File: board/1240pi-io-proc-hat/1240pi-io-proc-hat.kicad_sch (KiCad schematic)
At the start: 6 parts

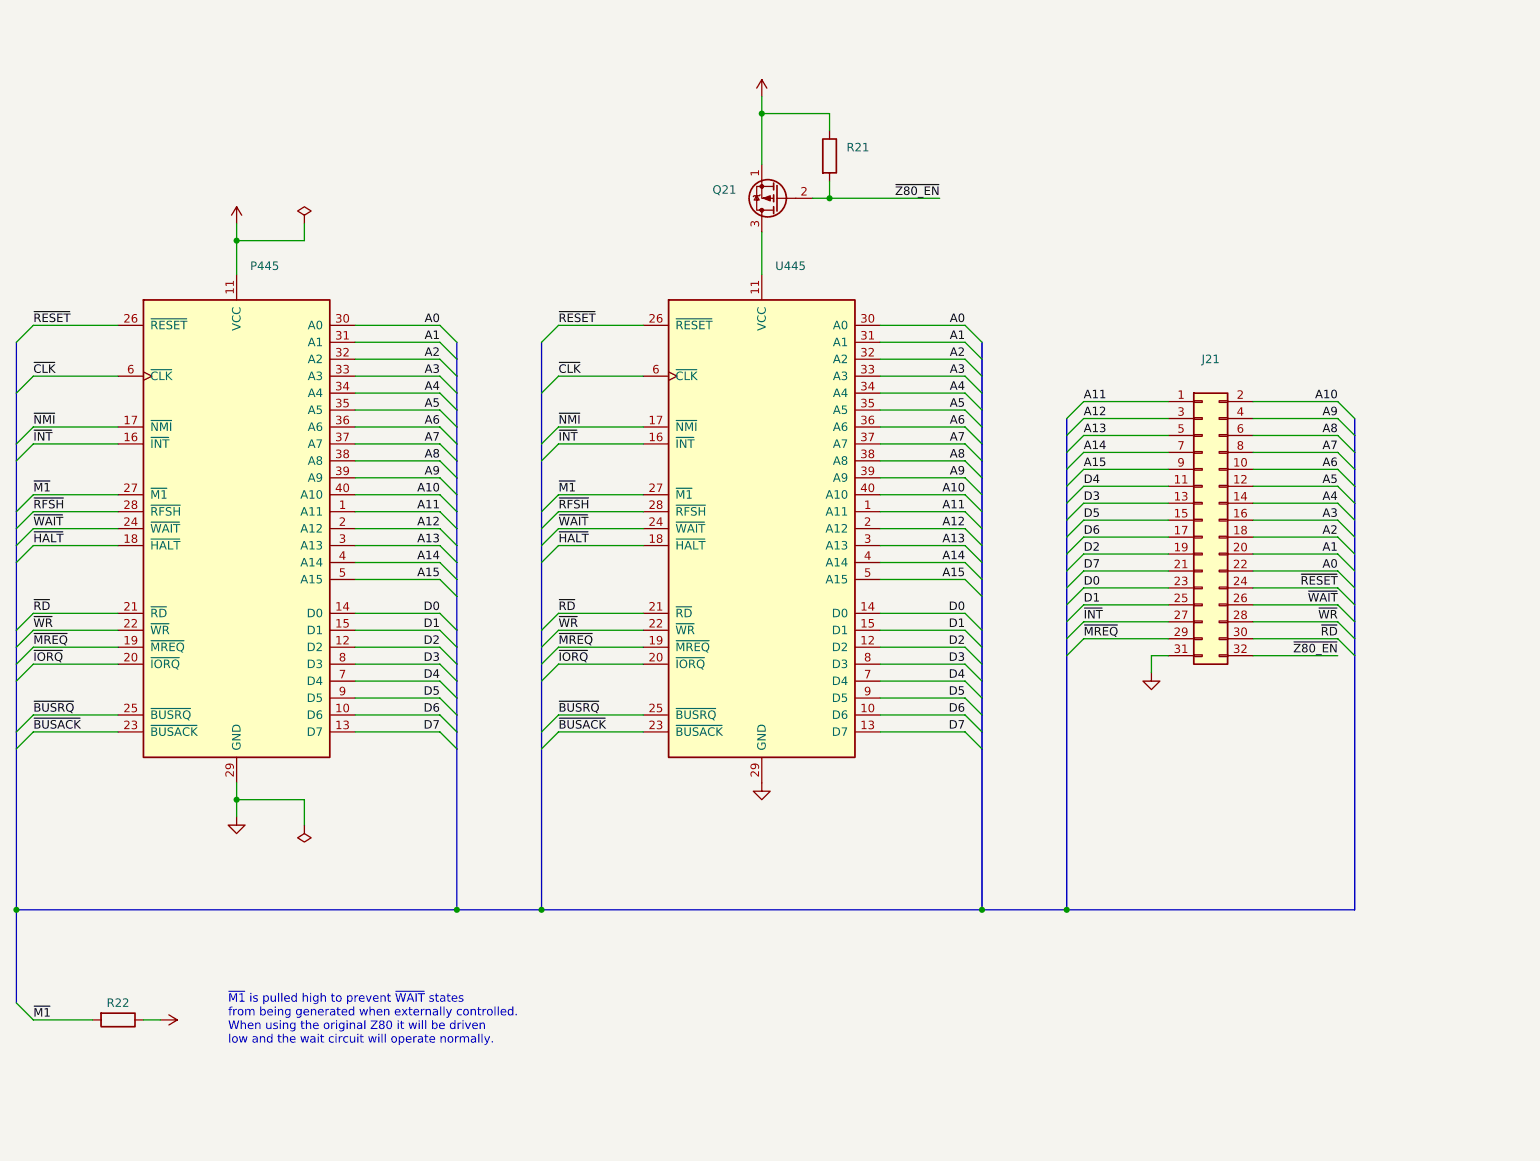
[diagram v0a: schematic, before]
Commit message: Split hats into separate projects / boards.
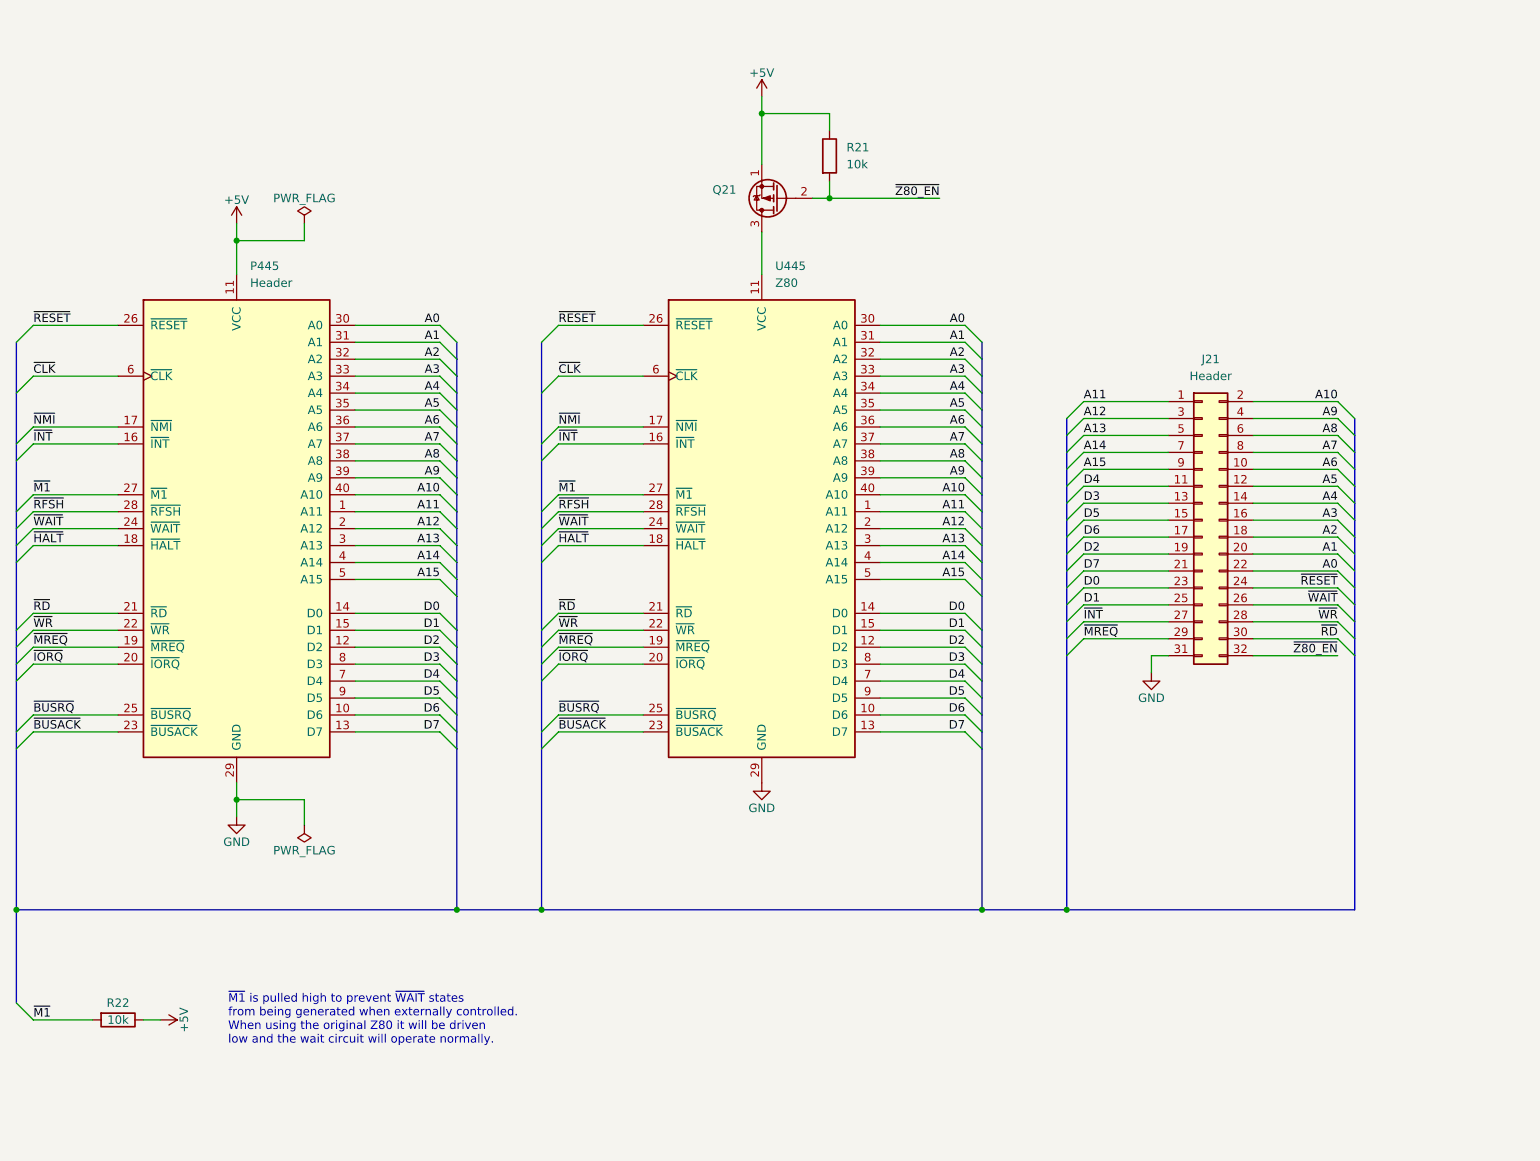
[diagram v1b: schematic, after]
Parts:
- J21: value (none) -> Header; footprint (none) -> Connector_PinHeader_2.54mm:PinHeader_2x16_P2.54mm_Vertical
- P445: value (none) -> Header; footprint (none) -> Package_DIP:DIP-40_W15.24mm
- Q21: value (none) -> ~; footprint (none) -> Package_TO_SOT_THT:TO-92_Wide
- R21, R22: value (none) -> 10k; footprint (none) -> Resistor_THT:R_Axial_DIN0207_L6.3mm_D2.5mm_P10.16mm_Horizontal
- U445: value (none) -> Z80; footprint (none) -> Package_DIP:DIP-40_W15.24mm_Socket
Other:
- title: 1240-Pi Modification Boards -> 1240-Pi I/O Processor Mod
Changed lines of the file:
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@@
   (paper "USLetter")
   (title_block
-    (title "1240-Pi Modification Boards")
+    (title "1240-Pi I/O Processor Mod")
     (date "2022-04-21")
     (rev "1.0")
@@
   (symbol (lib_id "power:GND") (at 195.58 129.54 0) (unit 1)
     (in_bom yes) (on_board yes) (fields_autoplaced)
-    (property "Reference" "#PWR0111" (id 0) (at 195.58 135.89 0)
-      (effects (font (size 1.27 1.27)) hide)
-    )
-    (property "Value" "" (id 1) (at 195.58 134.62 0))
+    (property "Reference" "#PWR?" (id 0) (at 195.58 135.89 0)
+      (effects (font (size 1.27 1.27)) hide)
+    )
+    (property "Value" "GND" (id 1) (at 195.58 133.35 0))
     (property "Footprint" "" (id 2) (at 195.58 129.54 0)
       (effects (font (size 1.27 1.27)) hide)
@@
   (symbol (lib_id "power:GND") (at 137.16 146.05 0) (unit 1)
     (in_bom yes) (on_board yes) (fields_autoplaced)
-    (property "Reference" "#PWR0106" (id 0) (at 137.16 152.4 0)
-      (effects (font (size 1.27 1.27)) hide)
-    )
-    (property "Value" "~" (id 1) (at 137.16 151.13 0))
+    (property "Reference" "#PWR?" (id 0) (at 137.16 152.4 0)
+      (effects (font (size 1.27 1.27)) hide)
+    )
+    (property "Value" "GND" (id 1) (at 137.16 149.86 0))
     (property "Footprint" "" (id 2) (at 137.16 146.05 0)
       (effects (font (size 1.27 1.27)) hide)
@@
       (effects (font (size 1.27 1.27)) (justify left))
     )
-    (property "Value" "" (id 1) (at 149.86 53.3399 0)
+    (property "Value" "10k" (id 1) (at 149.86 53.3399 0)
       (effects (font (size 1.27 1.27)) (justify left))
     )
-    (property "Footprint" "" (id 2) (at 145.542 52.07 90)
+    (property "Footprint" "Resistor_THT:R_Axial_DIN0207_L6.3mm_D2.5mm_P10.16mm_Horizontal" (id 2) (at 145.542 52.07 90)
       (effects (font (size 1.27 1.27)) hide)
     )
@@
       (effects (font (size 1.27 1.27)) (justify left))
     )
-    (property "Value" "" (id 1) (at 139.1794 71.12 0)
+    (property "Value" "Z80" (id 1) (at 139.1794 71.12 0)
       (effects (font (size 1.27 1.27)) (justify left))
     )
-    (property "Footprint" "" (id 2) (at 137.16 97.79 0)
+    (property "Footprint" "Package_DIP:DIP-40_W15.24mm_Socket" (id 2) (at 137.16 97.79 0)
       (effects (font (size 1.27 1.27)) hide)
     )
@@
   (symbol (lib_id "power:+5V") (at 46.99 181.61 270) (unit 1)
     (in_bom yes) (on_board yes) (fields_autoplaced)
-    (property "Reference" "#PWR0110" (id 0) (at 43.18 181.61 0)
-      (effects (font (size 1.27 1.27)) hide)
-    )
-    (property "Value" "" (id 1) (at 52.07 181.61 0))
+    (property "Reference" "#PWR?" (id 0) (at 43.18 181.61 0)
+      (effects (font (size 1.27 1.27)) hide)
+    )
+    (property "Value" "+5V" (id 1) (at 50.546 181.61 0))
     (property "Footprint" "" (id 2) (at 46.99 181.61 0)
       (effects (font (size 1.27 1.27)) hide)
@@
   (symbol (lib_id "power:+5V") (at 137.16 43.18 0) (unit 1)
     (in_bom yes) (on_board yes) (fields_autoplaced)
-    (property "Reference" "#PWR0107" (id 0) (at 137.16 46.99 0)
-      (effects (font (size 1.27 1.27)) hide)
-    )
-    (property "Value" "" (id 1) (at 137.16 38.1 0))
+    (property "Reference" "#PWR?" (id 0) (at 137.16 46.99 0)
+      (effects (font (size 1.27 1.27)) hide)
+    )
+    (property "Value" "+5V" (id 1) (at 137.16 39.624 0))
     (property "Footprint" "" (id 2) (at 137.16 43.18 0)
       (effects (font (size 1.27 1.27)) hide)
@@
   (symbol (lib_id "power:PWR_FLAG") (at 68.58 152.4 180) (unit 1)
     (in_bom yes) (on_board yes) (fields_autoplaced)
-    (property "Reference" "#FLG0103" (id 0) (at 68.58 154.305 0)
-      (effects (font (size 1.27 1.27)) hide)
-    )
-    (property "Value" "" (id 1) (at 68.58 157.48 0))
+    (property "Reference" "#FLG?" (id 0) (at 68.58 154.305 0)
+      (effects (font (size 1.27 1.27)) hide)
+    )
+    (property "Value" "PWR_FLAG" (id 1) (at 68.58 156.21 0))
     (property "Footprint" "" (id 2) (at 68.58 152.4 0)
       (effects (font (size 1.27 1.27)) hide)
@@
   (symbol (lib_id "power:GND") (at 58.42 151.13 0) (unit 1)
     (in_bom yes) (on_board yes) (fields_autoplaced)
-    (property "Reference" "#PWR0109" (id 0) (at 58.42 157.48 0)
-      (effects (font (size 1.27 1.27)) hide)
-    )
-    (property "Value" "" (id 1) (at 58.42 156.21 0))
+    (property "Reference" "#PWR?" (id 0) (at 58.42 157.48 0)
+      (effects (font (size 1.27 1.27)) hide)
+    )
+    (property "Value" "GND" (id 1) (at 58.42 154.94 0))
     (property "Footprint" "" (id 2) (at 58.42 151.13 0)
       (effects (font (size 1.27 1.27)) hide)
@@
       (effects (font (size 1.27 1.27)) (justify left))
     )
-    (property "Value" "" (id 1) (at 133.35 59.6899 0)
+    (property "Value" "~" (id 1) (at 133.35 59.6899 0)
       (effects (font (size 1.27 1.27)) (justify left))
     )
-    (property "Footprint" "" (id 2) (at 134.62 60.96 0)
+    (property "Footprint" "Package_TO_SOT_THT:TO-92_Wide" (id 2) (at 134.62 60.96 0)
       (effects (font (size 1.27 1.27)) hide)
     )
@@
   (symbol (lib_id "power:+5V") (at 58.42 62.23 0) (unit 1)
     (in_bom yes) (on_board yes) (fields_autoplaced)
-    (property "Reference" "#PWR0108" (id 0) (at 58.42 66.04 0)
-      (effects (font (size 1.27 1.27)) hide)
-    )
-    (property "Value" "" (id 1) (at 58.42 57.15 0))
+    (property "Reference" "#PWR?" (id 0) (at 58.42 66.04 0)
+      (effects (font (size 1.27 1.27)) hide)
+    )
+    (property "Value" "+5V" (id 1) (at 58.42 58.674 0))
     (property "Footprint" "" (id 2) (at 58.42 62.23 0)
       (effects (font (size 1.27 1.27)) hide)
@@
       (effects (font (size 1.27 1.27)) (justify left))
     )
-    (property "Value" "" (id 1) (at 60.4394 71.12 0)
+    (property "Value" "Header" (id 1) (at 60.4394 71.12 0)
       (effects (font (size 1.27 1.27)) (justify left))
     )
-    (property "Footprint" "" (id 2) (at 58.42 97.79 0)
+    (property "Footprint" "Package_DIP:DIP-40_W15.24mm" (id 2) (at 58.42 97.79 0)
       (effects (font (size 1.27 1.27)) hide)
     )
@@
   (symbol (lib_id "power:PWR_FLAG") (at 68.58 62.23 0) (unit 1)
     (in_bom yes) (on_board yes) (fields_autoplaced)
-    (property "Reference" "#FLG0104" (id 0) (at 68.58 60.325 0)
-      (effects (font (size 1.27 1.27)) hide)
-    )
-    (property "Value" "" (id 1) (at 68.58 57.15 0))
+    (property "Reference" "#FLG?" (id 0) (at 68.58 60.325 0)
+      (effects (font (size 1.27 1.27)) hide)
+    )
+    (property "Value" "PWR_FLAG" (id 1) (at 68.58 58.42 0))
     (property "Footprint" "" (id 2) (at 68.58 62.23 0)
       (effects (font (size 1.27 1.27)) hide)
@@
     (in_bom yes) (on_board yes)
     (property "Reference" "R22" (id 0) (at 40.64 179.07 90))
-    (property "Value" "" (id 1) (at 40.64 181.61 90))
-    (property "Footprint" "" (id 2) (at 40.64 179.832 90)
+    (property "Value" "10k" (id 1) (at 40.64 181.61 90))
+    (property "Footprint" "Resistor_THT:R_Axial_DIN0207_L6.3mm_D2.5mm_P10.16mm_Horizontal" (id 2) (at 40.64 179.832 90)
       (effects (font (size 1.27 1.27)) hide)
     )
@@
     (in_bom yes) (on_board yes) (fields_autoplaced)
     (property "Reference" "J21" (id 0) (at 204.47 82.55 0))
-    (property "Value" "" (id 1) (at 204.47 85.09 0))
-    (property "Footprint" "" (id 2) (at 203.2 106.68 0)
+    (property "Value" "Header" (id 1) (at 204.47 85.09 0))
+    (property "Footprint" "Connector_PinHeader_2.54mm:PinHeader_2x16_P2.54mm_Vertical" (id 2) (at 203.2 106.68 0)
       (effects (font (size 1.27 1.27)) hide)
     )
@@
     (pin "9")
   )
+  (sheet_instances
+    (path "/" (page "1"))
+  )
+  (symbol_instances
+    (path "/541631f1-5c6b-4984-b80b-da5d814ddc2a"
+      (reference "#FLG?") (unit 1) (value "PWR_FLAG") (footprint "")
+    )
+    (path "/b59ec72b-cbb3-4a84-b409-cb1a12e8909e"
+      (reference "#FLG?") (unit 1) (value "PWR_FLAG") (footprint "")
+    )
+    (path "/2aecf130-835d-43a0-a6c9-612e14e7a782"
+      (reference "#PWR?") (unit 1) (value "GND") (footprint "")
+    )
+    (path "/34c1fa01-b507-49e3-9b9f-c468b6e77596"
+      (reference "#PWR?") (unit 1) (value "GND") (footprint "")
+    )
+    (path "/53181a90-a010-4b72-99ae-37b5bd3dc882"
+      (reference "#PWR?") (unit 1) (value "+5V") (footprint "")
+    )
+    (path "/534827d0-458c-4104-bc6d-0255ad697b4c"
+      (reference "#PWR?") (unit 1) (value "+5V") (footprint "")
+    )
+    (path "/57c4d56d-de84-4172-ae0f-4c05a32da8d4"
+      (reference "#PWR?") (unit 1) (value "GND") (footprint "")
+    )
+    (path "/805d731d-4180-4b8e-bf12-b88ccec030b8"
+      (reference "#PWR?") (unit 1) (value "+5V") (footprint "")
+    )
+    (path "/f05fcee9-4158-40f8-b265-71b19b598390"
+      (reference "J21") (unit 1) (value "Header") (footprint "Connector_PinHeader_2.54mm:PinHeader_2x16_P2.54mm_Vertical")
+    )
+    (path "/8ad53c83-e421-4c0e-b4e0-361c324d4d58"
+      (reference "P445") (unit 1) (value "Header") (footprint "Package_DIP:DIP-40_W15.24mm")
+    )
+    (path "/6c1a4460-5fc9-4b10-afd6-ed10a018878d"
+      (reference "Q21") (unit 1) (value "~") (footprint "Package_TO_SOT_THT:TO-92_Wide")
+    )
+    (path "/39bc262a-7fca-4f46-a771-f7dcdf7ac0b0"
+      (reference "R21") (unit 1) (value "10k") (footprint "Resistor_THT:R_Axial_DIN0207_L6.3mm_D2.5mm_P10.16mm_Horizontal")
+    )
+    (path "/e1046c61-4f21-4849-8a9a-39f81b175891"
+      (reference "R22") (unit 1) (value "10k") (footprint "Resistor_THT:R_Axial_DIN0207_L6.3mm_D2.5mm_P10.16mm_Horizontal")
+    )
+    (path "/3a29e5d6-689f-46d7-a623-bc932a7056da"
+      (reference "U445") (unit 1) (value "Z80") (footprint "Package_DIP:DIP-40_W15.24mm_Socket")
+    )
+  )
 )

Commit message: Add hat boards to Aisler.
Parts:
- Q21: value ~ -> (none)
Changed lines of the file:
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@@
   (symbol (lib_id "power:GND") (at 195.58 129.54 0) (unit 1)
     (in_bom yes) (on_board yes) (fields_autoplaced)
-    (property "Reference" "#PWR?" (id 0) (at 195.58 135.89 0)
+    (property "Reference" "#PWR0104" (id 0) (at 195.58 135.89 0)
       (effects (font (size 1.27 1.27)) hide)
     )
@@
   (symbol (lib_id "power:GND") (at 137.16 146.05 0) (unit 1)
     (in_bom yes) (on_board yes) (fields_autoplaced)
-    (property "Reference" "#PWR?" (id 0) (at 137.16 152.4 0)
+    (property "Reference" "#PWR0106" (id 0) (at 137.16 152.4 0)
       (effects (font (size 1.27 1.27)) hide)
     )
@@
   (symbol (lib_id "power:+5V") (at 46.99 181.61 270) (unit 1)
     (in_bom yes) (on_board yes) (fields_autoplaced)
-    (property "Reference" "#PWR?" (id 0) (at 43.18 181.61 0)
+    (property "Reference" "#PWR0103" (id 0) (at 43.18 181.61 0)
       (effects (font (size 1.27 1.27)) hide)
     )
@@
   (symbol (lib_id "power:+5V") (at 137.16 43.18 0) (unit 1)
     (in_bom yes) (on_board yes) (fields_autoplaced)
-    (property "Reference" "#PWR?" (id 0) (at 137.16 46.99 0)
+    (property "Reference" "#PWR0105" (id 0) (at 137.16 46.99 0)
       (effects (font (size 1.27 1.27)) hide)
     )
@@
   (symbol (lib_id "power:PWR_FLAG") (at 68.58 152.4 180) (unit 1)
     (in_bom yes) (on_board yes) (fields_autoplaced)
-    (property "Reference" "#FLG?" (id 0) (at 68.58 154.305 0)
+    (property "Reference" "#FLG0102" (id 0) (at 68.58 154.305 0)
       (effects (font (size 1.27 1.27)) hide)
     )
@@
   (symbol (lib_id "power:GND") (at 58.42 151.13 0) (unit 1)
     (in_bom yes) (on_board yes) (fields_autoplaced)
-    (property "Reference" "#PWR?" (id 0) (at 58.42 157.48 0)
+    (property "Reference" "#PWR0102" (id 0) (at 58.42 157.48 0)
       (effects (font (size 1.27 1.27)) hide)
     )
@@
       (effects (font (size 1.27 1.27)) (justify left))
     )
-    (property "Value" "~" (id 1) (at 133.35 59.6899 0)
+    (property "Value" "" (id 1) (at 133.35 59.6899 0)
       (effects (font (size 1.27 1.27)) (justify left))
     )
@@
   (symbol (lib_id "power:+5V") (at 58.42 62.23 0) (unit 1)
     (in_bom yes) (on_board yes) (fields_autoplaced)
-    (property "Reference" "#PWR?" (id 0) (at 58.42 66.04 0)
+    (property "Reference" "#PWR0101" (id 0) (at 58.42 66.04 0)
       (effects (font (size 1.27 1.27)) hide)
     )
@@
   (symbol (lib_id "power:PWR_FLAG") (at 68.58 62.23 0) (unit 1)
     (in_bom yes) (on_board yes) (fields_autoplaced)
-    (property "Reference" "#FLG?" (id 0) (at 68.58 60.325 0)
+    (property "Reference" "#FLG0101" (id 0) (at 68.58 60.325 0)
       (effects (font (size 1.27 1.27)) hide)
     )
@@
   )
   (symbol_instances
+    (path "/b59ec72b-cbb3-4a84-b409-cb1a12e8909e"
+      (reference "#FLG0101") (unit 1) (value "PWR_FLAG") (footprint "")
+    )
     (path "/541631f1-5c6b-4984-b80b-da5d814ddc2a"
-      (reference "#FLG?") (unit 1) (value "PWR_FLAG") (footprint "")
-    )
-    (path "/b59ec72b-cbb3-4a84-b409-cb1a12e8909e"
-      (reference "#FLG?") (unit 1) (value "PWR_FLAG") (footprint "")
+      (reference "#FLG0102") (unit 1) (value "PWR_FLAG") (footprint "")
+    )
+    (path "/805d731d-4180-4b8e-bf12-b88ccec030b8"
+      (reference "#PWR0101") (unit 1) (value "+5V") (footprint "")
+    )
+    (path "/57c4d56d-de84-4172-ae0f-4c05a32da8d4"
+      (reference "#PWR0102") (unit 1) (value "GND") (footprint "")
+    )
+    (path "/53181a90-a010-4b72-99ae-37b5bd3dc882"
+      (reference "#PWR0103") (unit 1) (value "+5V") (footprint "")
     )
     (path "/2aecf130-835d-43a0-a6c9-612e14e7a782"
-      (reference "#PWR?") (unit 1) (value "GND") (footprint "")
+      (reference "#PWR0104") (unit 1) (value "GND") (footprint "")
+    )
+    (path "/534827d0-458c-4104-bc6d-0255ad697b4c"
+      (reference "#PWR0105") (unit 1) (value "+5V") (footprint "")
     )
     (path "/34c1fa01-b507-49e3-9b9f-c468b6e77596"
-      (reference "#PWR?") (unit 1) (value "GND") (footprint "")
-    )
-    (path "/53181a90-a010-4b72-99ae-37b5bd3dc882"
-      (reference "#PWR?") (unit 1) (value "+5V") (footprint "")
-    )
-    (path "/534827d0-458c-4104-bc6d-0255ad697b4c"
-      (reference "#PWR?") (unit 1) (value "+5V") (footprint "")
-    )
-    (path "/57c4d56d-de84-4172-ae0f-4c05a32da8d4"
-      (reference "#PWR?") (unit 1) (value "GND") (footprint "")
-    )
-    (path "/805d731d-4180-4b8e-bf12-b88ccec030b8"
-      (reference "#PWR?") (unit 1) (value "+5V") (footprint "")
+      (reference "#PWR0106") (unit 1) (value "GND") (footprint "")
     )
     (path "/f05fcee9-4158-40f8-b265-71b19b598390"
@@
     )
     (path "/6c1a4460-5fc9-4b10-afd6-ed10a018878d"
-      (reference "Q21") (unit 1) (value "~") (footprint "Package_TO_SOT_THT:TO-92_Wide")
+      (reference "Q21") (unit 1) (value "VP2106N3-G") (footprint "Package_TO_SOT_THT:TO-92_Wide")
     )
     (path "/39bc262a-7fca-4f46-a771-f7dcdf7ac0b0"
